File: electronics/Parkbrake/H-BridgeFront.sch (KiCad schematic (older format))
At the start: 82 parts

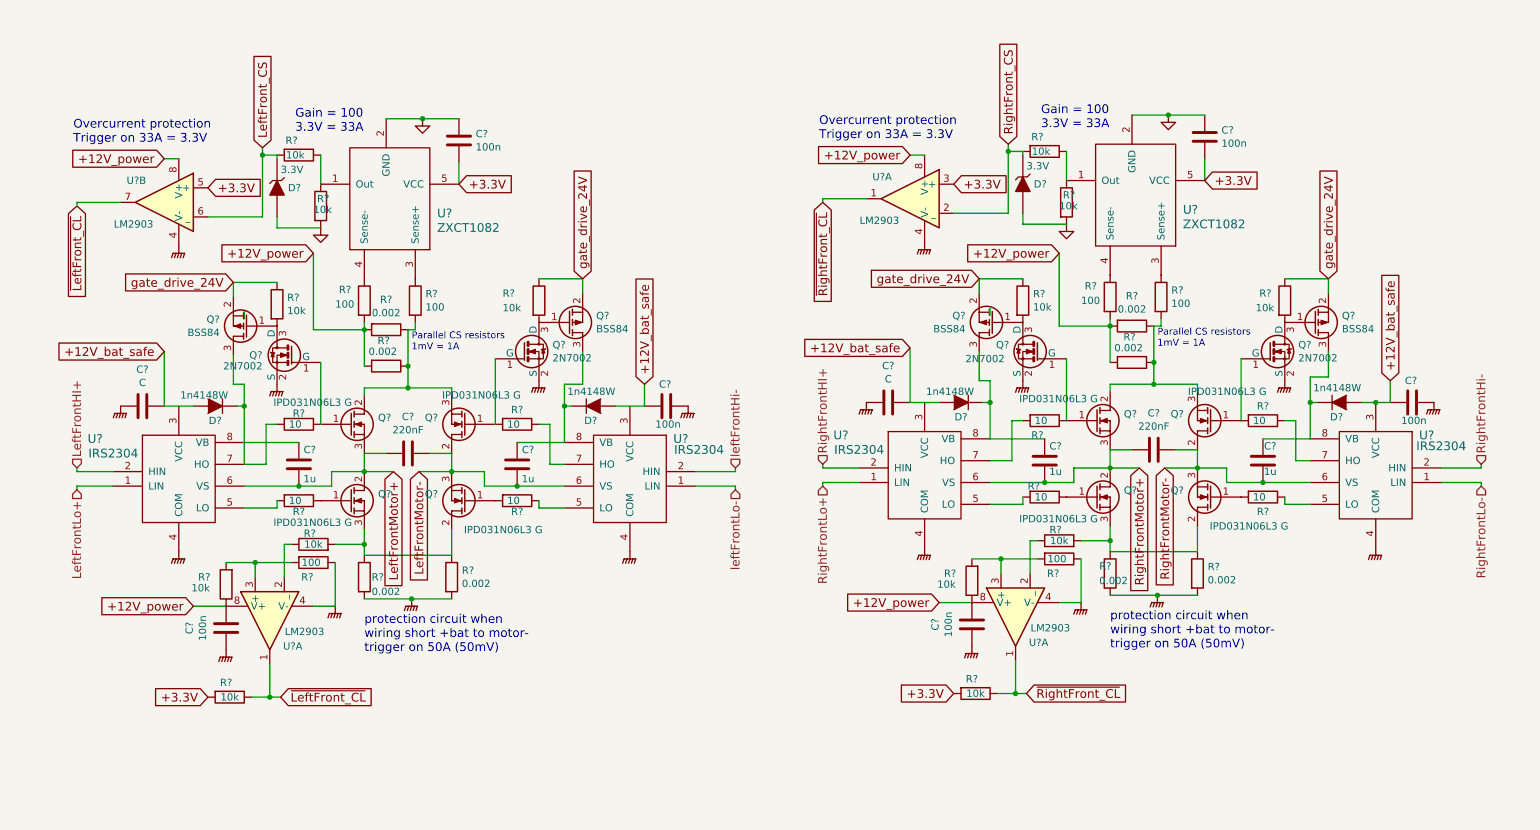
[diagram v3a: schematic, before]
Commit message: ordernr, type and footprints for all components
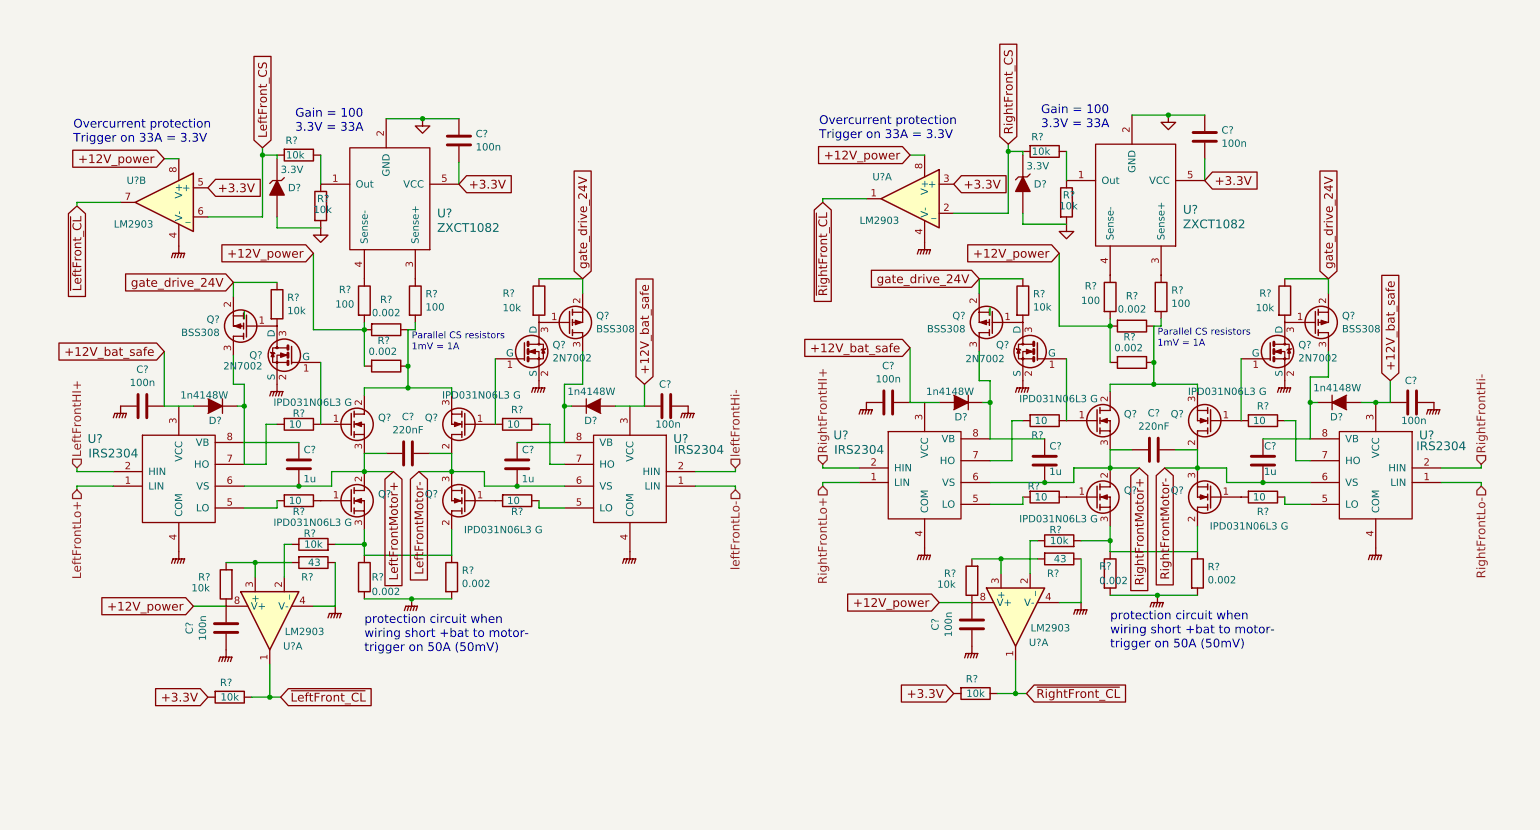
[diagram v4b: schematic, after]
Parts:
- C? (x2): footprint (none) -> Capacitors_SMD:C_1206; farnell (none) -> 2497088; part (none) -> 1206B224J500CT
- C? (x6): footprint (none) -> Capacitors_SMD:C_0805; farnell (none) -> 2496940; part (none) -> 0805B104J500CT
- C? (x4): footprint (none) -> Capacitors_SMD:C_1206; farnell (none) -> 2362126; part (none) -> GRM31MR71E105JA01L
- C? (x2): value C -> 100n; footprint (none) -> Capacitors_SMD:C_0805; farnell (none) -> 2496940; part (none) -> 0805B104J500CT
- D? (x4): footprint (none) -> Diodes_SMD:SOD-123; farnell (none) -> 2433353; part (none) -> 1N4148W-E3-08
- D? (x2): footprint (none) -> Diodes_SMD:SOD-123; farnell (none) -> 2454044; part (none) -> MMSZ4684
- Q? (x4): footprint (none) -> TO_SOT_Packages_SMD:TO-252-2Lead
- Q? (x4): footprint TO_SOT_Packages_SMD:SOT-23_Handsoldering -> TO_SOT_Packages_SMD:SOT-23
- Q? (x4): value BSS84 -> BSS308; footprint TO_SOT_Packages_SMD:SOT-23_Handsoldering -> TO_SOT_Packages_SMD:SOT-23; farnell 1510765 -> 2432719; part BSS84 -> BSS308PE H6327
- R? (x2): value 100 -> 43; footprint (none) -> Resistors_SMD:R_0805; farnell (none) -> 9333240; part (none) -> MC01W0805143R
- U?: farnell 1904025 -> 2496940

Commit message: Make it pass DRC rule check
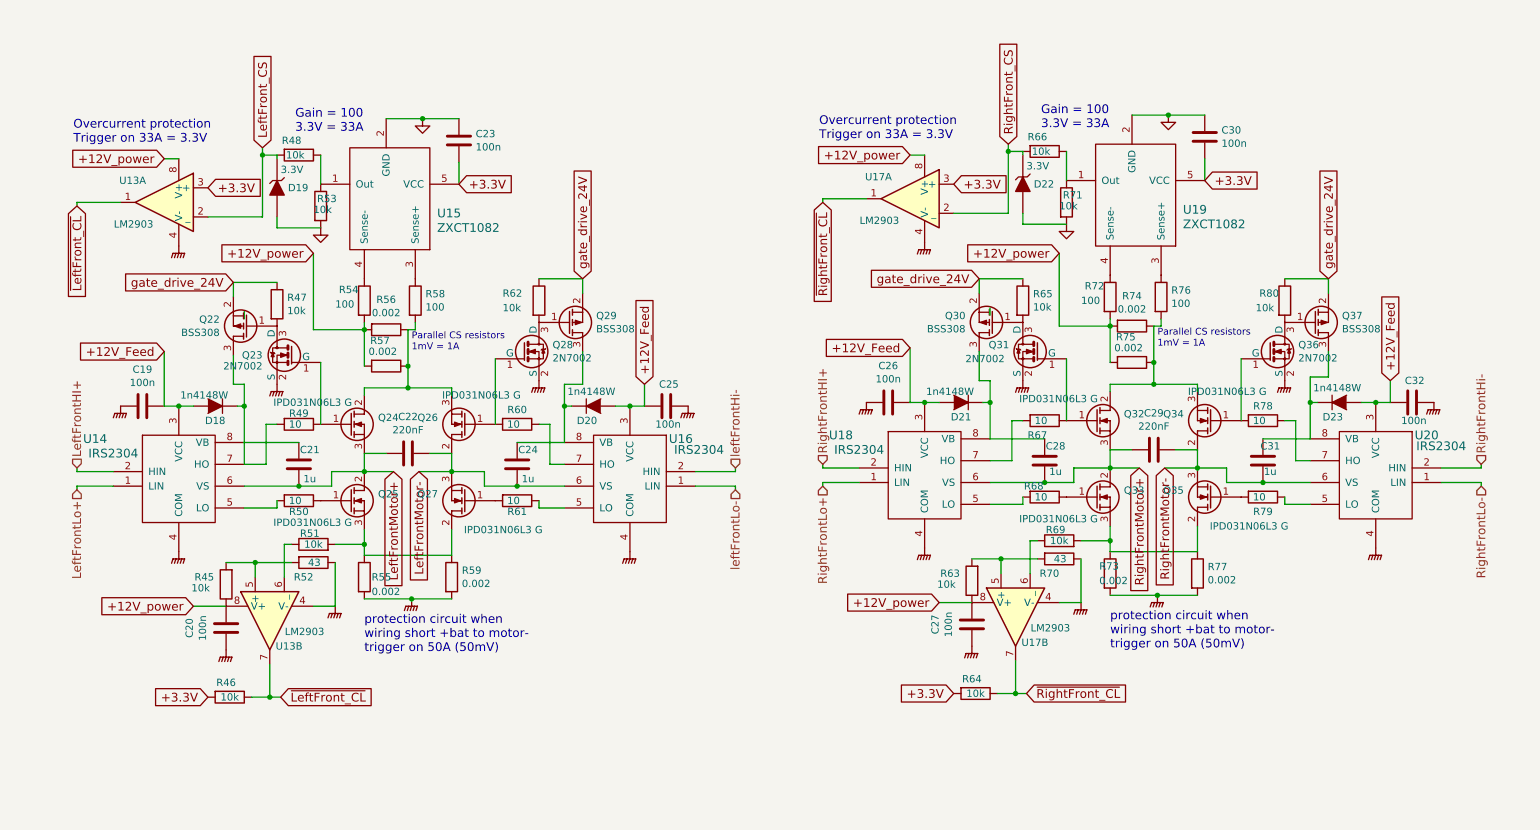
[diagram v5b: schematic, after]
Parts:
- removed C?: 220nF, Capacitors_SMD:C_1206, symbol C
- removed C? (x3): 100n, Capacitors_SMD:C_0805, symbol C
- removed C? (x3): 1u, Capacitors_SMD:C_1206, symbol C
- removed D?: 1n4148W, Diodes_SMD:SOD-123, symbol D
- removed Q? (x2): 2N7002, TO_SOT_Packages_SMD:SOT-23, symbol BSS138
- removed Q?: BSS308, TO_SOT_Packages_SMD:SOT-23, symbol Q_PMOS_GSD
- removed R? (x3): 0.002, Resistors_SMD:R_2512_HandSoldering, symbol R
- removed R? (x6): 10, Resistors_SMD:R_1206, symbol R
- removed R? (x5): 10k, Resistors_SMD:R_0805, symbol R
- removed R?: 100, Resistors_SMD:R_0805, symbol R
- removed U?: LM2903, symbol LM2903
- removed U?: IRS2304, symbol IRS2304
- added C22: 220nF, Capacitors_SMD:C_1206, symbol C
- added C23, C26, C32: 100n, Capacitors_SMD:C_0805, symbol C
- added C24, C28, C31: 1u, Capacitors_SMD:C_1206, symbol C
- added D23: 1n4148W, Diodes_SMD:SOD-123, symbol D
- added Q28, Q31: 2N7002, TO_SOT_Packages_SMD:SOT-23, symbol BSS138
- added Q30: BSS308, TO_SOT_Packages_SMD:SOT-23, symbol Q_PMOS_GSD
- added R49, R50, R60, R61, R67, R78: 10, Resistors_SMD:R_1206, symbol R
- added R51, R65, R66, R71, R80: 10k, Resistors_SMD:R_0805, symbol R
- added R59, R74, R77: 0.002, Resistors_SMD:R_2512_HandSoldering, symbol R
- added R72: 100, Resistors_SMD:R_0805, symbol R
- added unit 2 of U13
- added U16: IRS2304, symbol IRS2304
- gave numbers to parts that had none: 53
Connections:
- net +12V_bat_safe is gone; now on net +12V_Feed: C19.1, C25.2, D18.2 (A), D20.2 (A), D21.2 (A), U20.3 (VCC)
- net +12V_power: now also R72.2, R74.2, U13.8 (V+)
- net +3.3V: now also U13.3 (+), C23.2; no longer U13.5 (+)
- net GND: now also C23.1, R71.2
- net GNDPWR: now also C26.2, C32.1, Q28.2 (S), Q31.2 (S), R59.2, R77.2, U13.4 (V-), U16.4 (COM)
- net LeftFrontMotor+: now also C22.2
- net LeftFrontMotor-: now also C22.1, C24.1, U16.6 (VS)
- net LeftFront_CS: now also U13.2 (_); no longer U13.6 (_)
- net RightFrontMotor+: now also C28.1
- net RightFrontMotor-: now also C31.2
- net RightFront_CS: now also R66.2
- net gate_drive_24V: now also Q30.2 (S), R65.1, R80.1
- net leftFrontHi-: now also U16.2 (HIN)
- net leftFrontLo-: now also U16.1 (LIN)
- net ~LeftFront_CL: now also U13.1, U13.7; no longer U13.7
- net ~RightFront_CL: now also U17.7; no longer U17.1
- net at Q25.1 (G): now also R50.1
- net at Q25.3 (S), Q27.2 (D), R55.1: now also R51.2, R59.1
- net at Q27.1 (G): now also R61.2
- net at Q26.1 (G): now also Q28.1 (G), R60.2
- net at Q23.1 (G), Q24.1 (G): now also R49.1
- net at U14.5 (LO): now also R50.2
- net at D18.1 (K), Q22.3 (D), U14.7 (HO): now also R49.2
- net at D20.1 (K), Q29.3 (D): now also C24.2, U16.8 (VB)
- net at Q29.1 (G), R62.2: now also Q28.3 (D)
- net at R45.2, R52.2: now also U13.5 (+)
- net +12V_Feed: now reaches U14.3 (VCC)
- net +12V_Feed: now also U18.3 (VCC), C26.1, C32.2, D23.2 (A), U16.3 (VCC)
- net at Q33.3 (S), Q35.2 (D), R69.2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: now also R77.1
- net at Q34.1 (G), Q36.1 (G): now also R78.2
- net at Q32.2 (D), Q34.3 (S), R75.1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: now also R74.1
- net at Q32.1 (G): now also Q31.1 (G), R67.1
- net at U19.1 (Out): now also R66.1, R71.1
- net at U19.4 (Sense-): now also R72.1
- net at U18.7 (HO): now also R67.2
- net at U20.7 (HO): now also R78.1
- net at Q37.3 (D), U20.8 (VB): now also C31.1, D23.1 (K)
- net at Q36.3 (D), Q37.1 (G): now also R80.2
- net at D21.1 (K), U18.8 (VB): now also C28.2, Q30.3 (D)
- net at R63.2, R70.2: now also U17.5 (+); no longer U17.3 (+)
- net at R69.1: now also U17.6 (_); no longer U17.2 (_)
- new net: R61.1, U16.5 (LO)
- new net: R60.1, U16.7 (HO)
- new net: R51.1, U13.6 (_)
- new net: Q30.1 (G), Q31.3 (D), R65.2

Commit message: More fixes and chenged components eat less boardspace
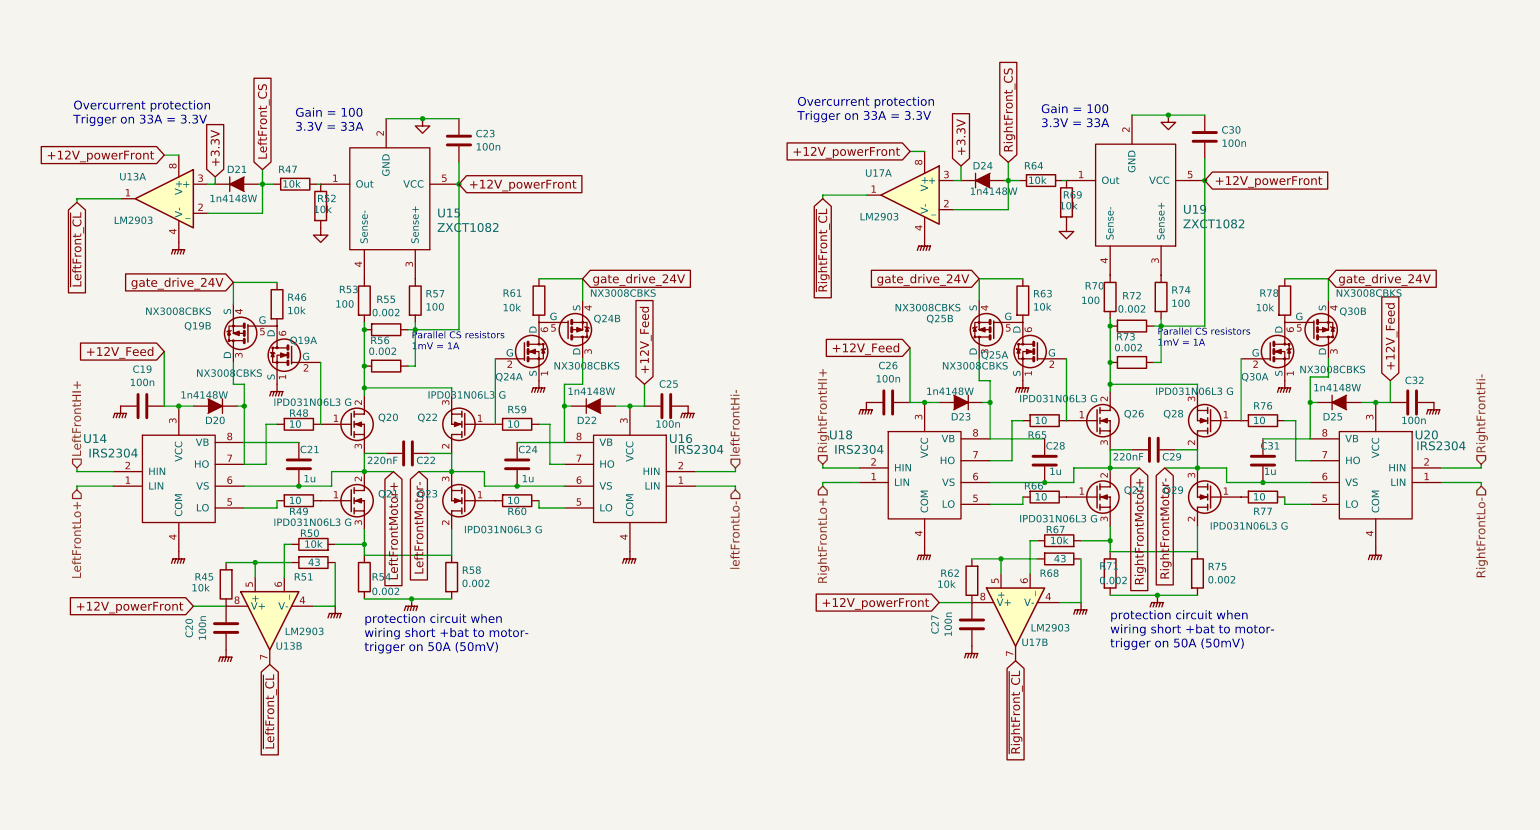
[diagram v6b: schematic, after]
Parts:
- removed D19, D22: 3.3V, Diodes_SMD:SOD-123, symbol ZENER
- removed Q22, Q29, Q30, Q37: BSS308, TO_SOT_Packages_SMD:SOT-23, symbol Q_PMOS_GSD
- removed Q23, Q28, Q31, Q36: 2N7002, TO_SOT_Packages_SMD:SOT-23, symbol BSS138
- removed R46, R64: 10k, Resistors_SMD:R_0805, symbol R
- added D21, D24: 1n4148W, Diodes_SMD:SOD-323, symbol D
- added Q19, Q24, Q25, Q30: NX3008CBKS, SOT363:SOT-363, symbol NX3008CBKS
- D20: renamed from D18; footprint Diodes_SMD:SOD-123 -> Diodes_SMD:SOD-323; farnell 2433353 -> 1466524; part 1N4148W-E3-08 -> 1N4148WS
- D22: renamed from D20; footprint Diodes_SMD:SOD-123 -> Diodes_SMD:SOD-323; farnell 2433353 -> 1466524; part 1N4148W-E3-08 -> 1N4148WS
- D23: renamed from D21; footprint Diodes_SMD:SOD-123 -> Diodes_SMD:SOD-323; part 1N4148W-E3-08 -> 1N4148WS
- D25: renamed from D23; footprint Diodes_SMD:SOD-123 -> Diodes_SMD:SOD-323; farnell 2433353 -> 1466524; part 1N4148W-E3-08 -> 1N4148WS
- R54: renamed from R55; footprint Resistors_SMD:R_2512_HandSoldering -> Resistors_SMD:R_1206; farnell 2079420 -> 1621962; part LRMAT2512-R002FT4 -> ULR1S-R002FT2
- R55: renamed from R56; footprint Resistors_SMD:R_2512_HandSoldering -> Resistors_SMD:R_1206; farnell 2079420 -> 1621962; part LRMAT2512-R002FT4 -> ULR1S-R002FT2
- R56: renamed from R57; footprint Resistors_SMD:R_2512_HandSoldering -> Resistors_SMD:R_1206; farnell 2079420 -> 1621962; part LRMAT2512-R002FT4 -> ULR1S-R002FT2
- R57: renamed from R58; farnell MC01W08051100R -> 9332375; part 9332375 -> MC01W08051100R
- R58: renamed from R59; footprint Resistors_SMD:R_2512_HandSoldering -> Resistors_SMD:R_1206; farnell 2079420 -> 1621962; part LRMAT2512-R002FT4 -> ULR1S-R002FT2
- R69: renamed from R71; farnell (none) -> 9332391
- R70: renamed from R72; farnell MC01W08051100R -> 9332375; part 9332375 -> MC01W08051100R
- R71: renamed from R73; footprint Resistors_SMD:R_2512_HandSoldering -> Resistors_SMD:R_1206; farnell 2079420 -> 1621962; part LRMAT2512-R002FT4 -> ULR1S-R002FT2
- R72: renamed from R74; footprint Resistors_SMD:R_2512_HandSoldering -> Resistors_SMD:R_1206; farnell 2079420 -> 1621962; part LRMAT2512-R002FT4 -> ULR1S-R002FT2
- R73: renamed from R75; footprint Resistors_SMD:R_2512_HandSoldering -> Resistors_SMD:R_1206; farnell 2079420 -> 1621962; part LRMAT2512-R002FT4 -> ULR1S-R002FT2
- R74: renamed from R76; farnell MC01W08051100R -> 9332375; part 9332375 -> MC01W08051100R
- R75: renamed from R77; footprint Resistors_SMD:R_2512_HandSoldering -> Resistors_SMD:R_1206; farnell 2079420 -> 1621962; part LRMAT2512-R002FT4 -> ULR1S-R002FT2
- U13, U17: footprint (none) -> Housings_SSOP:TSSOP-8_4.4x3mm_Pitch0.65mm; farnell (none) -> 1094243; part (none) -> LM2903PT
- U14, U16, U18, U20: footprint (none) -> Housings_SOIC:SOIC-8_3.9x4.9mm_Pitch1.27mm; farnell (none) -> 1498208; part (none) -> IRS2304SPBF
- U15: farnell 2496940 -> 1904025
- renumbered Q24 to Q20, Q25 to Q21, Q26 to Q22, Q27 to Q23, Q32 to Q26, Q33 to Q27, Q34 to Q28, Q35 to Q29, R47 to R46, R48 to R47, R49 to R48, R50 to R49, R51 to R50, R52 to R51, R53 to R52, R54 to R53, R60 to R59, R61 to R60, R62 to R61, R63 to R62, R65 to R63, R66 to R64, R67 to R65, R68 to R66, R69 to R67, R70 to R68, R78 to R76, R79 to R77, R80 to R78
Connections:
- net +3.3V: now also D21.1 (K), D24.1 (K); no longer C23.2, C30.2, U15.5 (VCC), U19.5 (VCC)
- net GNDPWR: now also Q19.1 (S), Q24.1 (S), Q25.1 (S), Q30.1 (S)
- net LeftFront_CS: now also D21.2 (A)
- net RightFront_CS: now also D24.2 (A)
- net gate_drive_24V: now also Q19.4 (S), Q24.4 (S), Q25.4 (S), Q30.4 (S)
- net at Q22.1 (G), R59.2: now also Q24.2 (G)
- net +12V_powerFront: now reaches R55.1, R56.1, R57.2
- net +12V_powerFront: now also C20.1, C23.2, C27.1, C30.2, R45.1, R62.1, R72.1, R73.1, R74.2, U13.8 (V+), U13.8 (V+), U15.5 (VCC), U17.8 (V+), U17.8 (V+), U19.5 (VCC); no longer Q20.2 (D), Q22.3 (S)
- net at Q20.1 (G), R48.1: now also Q19.2 (G)
- net at C24.2, D22.1 (K), U16.8 (VB): now also Q24.3 (D)
- net at D20.1 (K), R48.2, U14.7 (HO): now also Q19.3 (D)
- net at R46.2: now also Q19.5 (G), Q19.6 (D)
- net at Q28.1 (G), R76.2: now also Q30.2 (G)
- net at Q26.1 (G), R65.1: now also Q25.2 (G)
- net at R78.2: now also Q30.5 (G), Q30.6 (D)
- net at C28.2, D23.1 (K), U18.8 (VB): now also Q25.3 (D)
- net at R61.2: now also Q24.5 (G), Q24.6 (D)
- net at C31.1, D25.1 (K), U20.8 (VB): now also Q30.3 (D)
- net at R63.2: now also Q25.5 (G), Q25.6 (D)
- removed net +12V_power: C20.1, C27.1, R45.1, R53.2, R55.2, R56.2, R62.1, R70.2, R72.2, R73.2, U13.8 (V+), U13.8 (V+), U17.8 (V+), U17.8 (V+)
- new net: Q20.2 (D), Q22.3 (S), R53.2, R55.2, R56.2
- new net: Q26.2 (D), Q28.3 (S), R70.2, R72.2, R73.2
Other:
- moved on the sheet: R47, R64, U13A, U17A

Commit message: some more work on parkbrake pcb
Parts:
- R48, R49, R59, R60, R65, R66, R76, R77: footprint Resistors_SMD:R_1206 -> Resistors_SMD:R_0805; farnell 9335790 -> 2502783; part MC0125W1206110R -> WF08P10R0FTL
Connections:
- net +12V_Feed is gone; now on net +12V_powerFront: C19.1, C25.2, C26.1, C32.2, D20.2 (A), D22.2 (A), D23.2 (A), D25.2 (A), U14.3 (VCC), U16.3 (VCC), U18.3 (VCC), U20.3 (VCC)
- net GND is gone; now on net GNDPWR: C23.1, C30.1, R52.2, R69.2, U15.2 (GND), U19.2 (GND)
- net LeftFrontMotor-: now also Q22.3 (S), Q23.2 (D); no longer Q22.2 (D), Q23.3 (S)
- net RightFrontMotor-: now also Q28.3 (S), Q29.2 (D); no longer Q28.2 (D), Q29.3 (S)
- net at Q21.3 (S), R50.2, R54.1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: now also Q23.3 (S); no longer Q23.2 (D)
- net at Q20.2 (D), R53.2, R55.2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: now also Q22.2 (D); no longer Q22.3 (S)
- net at Q27.3 (S), R67.2, R71.1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: now also Q29.3 (S); no longer Q29.2 (D)
- net at Q26.2 (D), R70.2, R72.2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: now also Q28.2 (D); no longer Q28.3 (S)
